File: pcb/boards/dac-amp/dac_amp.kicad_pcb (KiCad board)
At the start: 2 copper layers, 65 x 56 mm, 49 parts, among them J1 I2S_Input, J2 12V_Input, J3 Front_Left, J4 Front_Right, J5 Rear_Left, J6 Rear_Right, J7 40-Pin_GPIO, U1 PCM5142, U2 AMS1117-3.3, U3 TPA3116D2, U4 TPA3116D2

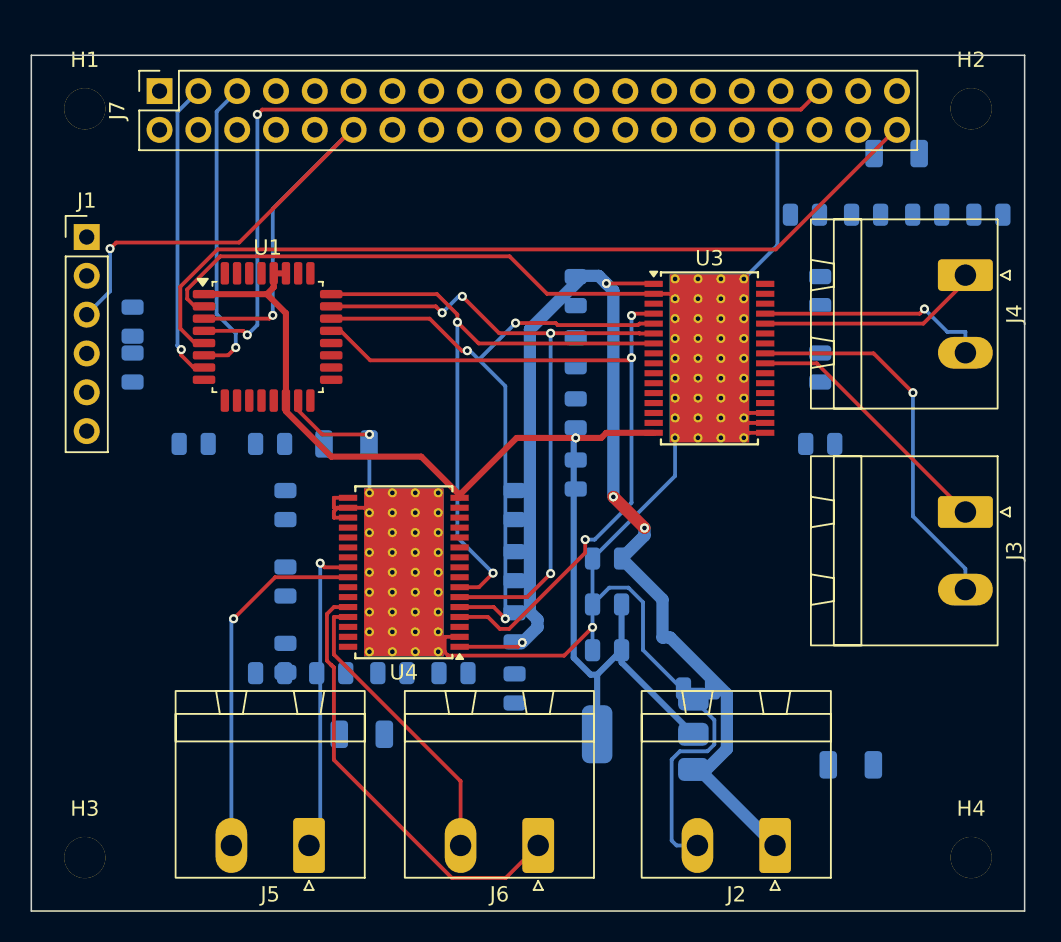
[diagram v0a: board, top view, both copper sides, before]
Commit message: DAC/Amp HAT PCB: Ready for PCBA manufacturing
- PCB fully routed via FreeRouting auto-router
- DRC clean: 0 unconnected pads, 0 errors (warnings are cosmetic)
- Power traces widened: +12V @ 1.0mm, speaker outputs @ 0.75mm
- Thermal vias added under U3 and U4 (6-8 vias each)
- Fiducials added for pick-and-place assembly
- GND copper pour on back layer for thermal dissipation
- BOM with manufacturer part numbers (dac_amp_bom.csv)
- Gerbers and placement files generated for PCBWay

Manufacturing notes:
- Recommend 2oz copper for power handling
- ENIG surface finish for PCBA
- Double-sided assembly (components on front and back)

Co-Authored-By: Claude Opus 4.5 <noreply@anthropic.com>
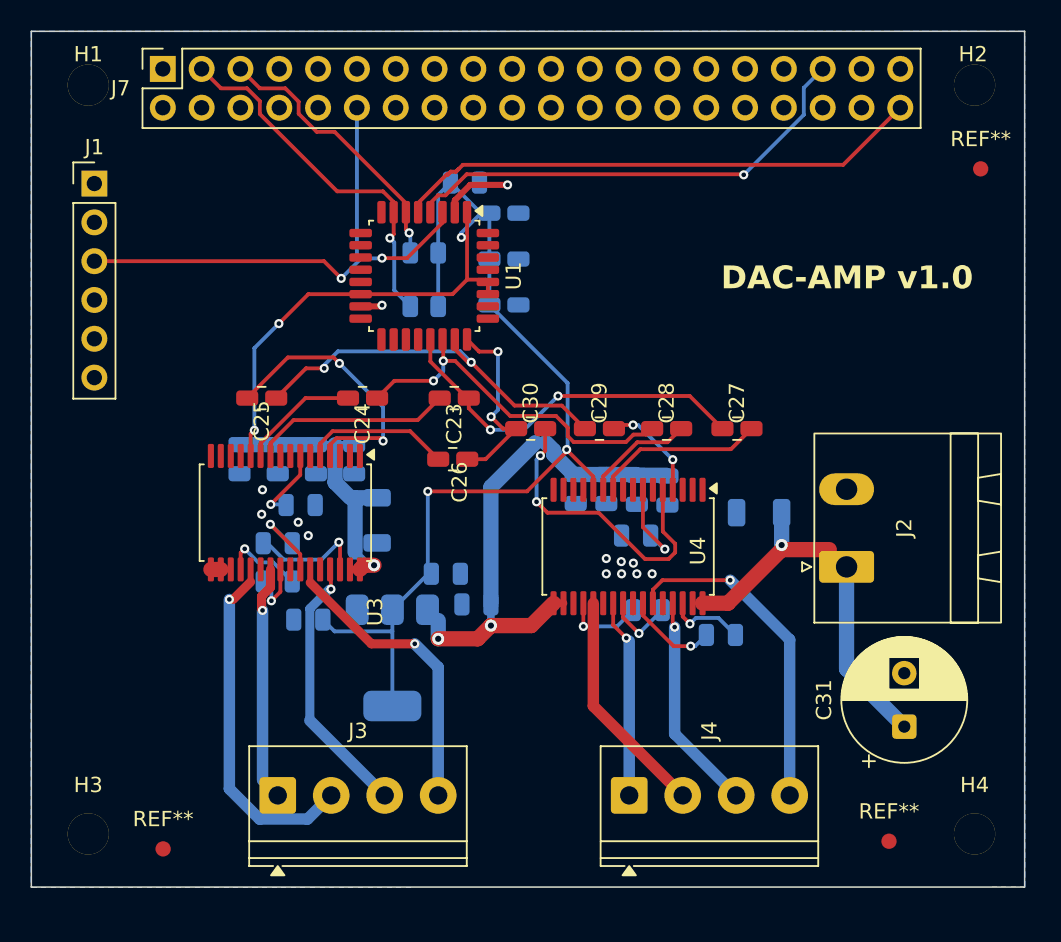
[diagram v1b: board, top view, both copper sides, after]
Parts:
- removed J5: Rear_Left, Connector_Phoenix_MSTB:PhoenixContact_MSTBA_2,5_2-G-5,08_1x02_P5.08mm_Horizontal
- removed J6: Rear_Right, Connector_Phoenix_MSTB:PhoenixContact_MSTBA_2,5_2-G-5,08_1x02_P5.08mm_Horizontal
- added REF**: Fiducial_1mm_Mask2mm, Fiducial:Fiducial_1mm_Mask2mm, F.Cu at (157.5, 86.0)
- added REF**: Fiducial_1mm_Mask2mm, Fiducial:Fiducial_1mm_Mask2mm, F.Cu at (110.0, 86.5)
- added REF**: Fiducial_1mm_Mask2mm, Fiducial:Fiducial_1mm_Mask2mm, F.Cu at (163.5, 42.0)
- C10, C11, C12, C13, C14, C15, C16, C17, C18, C19, C20, C21, C22, C32, C4, C5, C7, C8, C9, R1, R2: moved to F.Cu
- C31: footprint Capacitor_SMD:C_1206_3216Metric -> Capacitor_THT:CP_Radial_D8.0mm_P3.50mm; moved to F.Cu
- C6: footprint Capacitor_SMD:C_1206_3216Metric -> Capacitor_SMD:C_0805_2012Metric; moved to F.Cu
- J3: value Front_Left -> Conn_01x04; footprint Connector_Phoenix_MSTB:PhoenixContact_MSTBA_2,5_2-G-5,08_1x02_P5.08mm_Horizontal -> TerminalBlock_Phoenix:TerminalBlock_Phoenix_PT-1,5-4-3.5-H_1x04_P3.50mm_Horizontal
- J4: value Front_Right -> Conn_01x04; footprint Connector_Phoenix_MSTB:PhoenixContact_MSTBA_2,5_2-G-5,08_1x02_P5.08mm_Horizontal -> TerminalBlock_Phoenix:TerminalBlock_Phoenix_PT-1,5-4-3.5-H_1x04_P3.50mm_Horizontal
- U3, U4: value TPA3116D2 -> TPA3116D2DAD; footprint Package_SO:HTSSOP-32-1EP_6.1x11mm_P0.65mm_EP5.2x11mm_Mask4.11x4.36mm_ThermalVias -> Package_SO:Texas_DAD0032A_HTSSOP-32_6.1x11mm_P0.65mm_TopEP3.71x3.81mm
- moved J3 48.7 mm to (117.5, 83.0), turned to 0 degrees
- moved C14 44.5 mm to (122.5, 61.0), turned to -90 degrees
- moved C13 43.1 mm to (120.0, 61.0), turned to -90 degrees
- moved C12 41.7 mm to (117.5, 61.0), turned to -90 degrees
- moved C19 41.6 mm to (124.0, 65.0), turned to -90 degrees
- moved J4 40.5 mm to (140.5, 83.0), turned to 0 degrees
- moved C11 40.3 mm to (115.0, 61.0), turned to -90 degrees
- moved C7 40.3 mm to (117.5, 69.0), turned to 0 degrees
- moved C8 37.3 mm to (117.5, 66.5), turned to 0 degrees
- moved C21 34.2 mm to (119.0, 64.0)
- moved C20 29.8 mm to (149.0, 64.5), turned to 180 degrees
- moved U3 29.5 mm to (118.0, 64.5), turned to -90 degrees
- moved C2 29.1 mm to (129.8, 42.9), turned to 0 degrees
- moved C10 28.7 mm to (146.5, 72.5), turned to 180 degrees
- moved C9 24.7 mm to (141.7, 70.9), turned to 180 degrees
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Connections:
- C1 pad 1: +12V -> /+12V
- C10 pad 1: (no net) -> /U4_BSPR
- C10 pad 2: (no net) -> /U4_BSNR
- C11 pad 1: (no net) -> /+12V
- C11 pad 2: (no net) -> GND
- C12 pad 1: (no net) -> /+12V
- C12 pad 2: (no net) -> GND
- C13 pad 1: (no net) -> /+12V
- C13 pad 2: (no net) -> GND
- C14 pad 1: (no net) -> /+12V
- C14 pad 2: (no net) -> GND
- C15 pad 1: (no net) -> /+12V
- C15 pad 2: (no net) -> GND
- C16 pad 1: (no net) -> /+12V
- C16 pad 2: (no net) -> GND
- C17 pad 1: (no net) -> /+12V
- C17 pad 2: (no net) -> GND
- C18 pad 1: (no net) -> /+12V
- C18 pad 2: (no net) -> GND
- C19 pad 1: (no net) -> /+12V
- C19 pad 2: (no net) -> GND
- C20 pad 1: (no net) -> /+12V
- C20 pad 2: (no net) -> GND
- C21 pad 1: (no net) -> /U3_GVDD
- C21 pad 2: (no net) -> GND
- C22 pad 1: (no net) -> /U4_GVDD
- C22 pad 2: (no net) -> GND
- C23 pad 1: (no net) -> /DAC_OUTL+
- C23 pad 2: (no net) -> /U3_LINP
- C24 pad 1: (no net) -> /DAC_OUTL-
- C24 pad 2: (no net) -> /U3_LINN
- C25 pad 1: (no net) -> /DAC_OUTR+
- C25 pad 2: (no net) -> /U3_RINP
- C26 pad 1: (no net) -> /DAC_OUTR-
- C26 pad 2: (no net) -> /U3_RINN
- C27 pad 1: (no net) -> /DAC_OUTL+
- C27 pad 2: (no net) -> /U4_LINP
- C28 pad 1: (no net) -> /DAC_OUTL-
- C28 pad 2: (no net) -> /U4_LINN
- C29 pad 1: (no net) -> /DAC_OUTR+
- C29 pad 2: (no net) -> /U4_RINP
- C30 pad 1: (no net) -> /DAC_OUTR-
- C30 pad 2: (no net) -> /U4_RINN
- C31 pad 1: (no net) -> /+12V
- C31 pad 2: (no net) -> GND
- C32 pad 1: (no net) -> +3.3V
- C32 pad 2: (no net) -> GND
- C4 pad 1: (no net) -> +3.3V
- C4 pad 2: (no net) -> GND
- C5 pad 1: (no net) -> +3.3V
- C5 pad 2: (no net) -> GND
- C6 pad 1: (no net) -> +3.3V
- C6 pad 2: (no net) -> GND
- C7 pad 1: (no net) -> /U3_BSPL
- C7 pad 2: (no net) -> /U3_BSNL
- C8 pad 1: (no net) -> /U3_BSPR
- C8 pad 2: (no net) -> /U3_BSNR
- C9 pad 1: (no net) -> /U4_BSPL
- C9 pad 2: (no net) -> /U4_BSNL
- J2 pad 1: +12V -> /+12V
- J3 pad 1: Net-(J3-Pin_1) -> /U3_OUTPL
- J3 pad 2: Net-(J3-Pin_2) -> /U3_OUTNL
- J4 pad 1: Net-(J4-Pin_1) -> /U4_OUTPL
- J4 pad 2: Net-(J4-Pin_2) -> /U4_OUTNL
- R1 pad 1: (no net) -> +3.3V
- R1 pad 2: (no net) -> I2C_SCL
- R2 pad 1: (no net) -> +3.3V
- R2 pad 2: (no net) -> I2C_SDA
- U1 pad 21: Net-(U1-OUTL+) -> /DAC_OUTL+
- U1 pad 22: Net-(U1-OUTL-) -> /DAC_OUTL-
- U1 pad 23: Net-(U1-OUTR+) -> /DAC_OUTR+
- U1 pad 24: Net-(U1-OUTR-) -> /DAC_OUTR-
- U2 pad 3: +12V -> /+12V
- U3 pad 1: +12V -> GND
- U3 pad 10: (no net) -> /U3_LINP
- U3 pad 11: (no net) -> /U3_LINN
- U3 pad 12: (no net) -> +3.3V
- U3 pad 13: (no net) -> GND
- U3 pad 14: (no net) -> GND
- U3 pad 15: (no net) -> GND
- U3 pad 16: +3.3V -> unconnected-(U3-SYNC-Pad16)
- U3 pad 17: GND -> /+12V
- U3 pad 18: GND -> /+12V
- U3 pad 19: GND -> /+12V
- U3 pad 2: GND -> /+12V
- U3 pad 20: (no net) -> /U3_BSNL
- U3 pad 21: (no net) -> /U3_OUTNL
- U3 pad 22: (no net) -> GND
- U3 pad 23: (no net) -> /U3_OUTPL
- U3 pad 24: Net-(J3-Pin_1) -> /U3_BSPL
- U3 pad 25: Net-(J3-Pin_2) -> GND
- U3 pad 26: (no net) -> /U3_BSNR
- U3 pad 27: (no net) -> /U3_OUTNR
- U3 pad 28: Net-(J4-Pin_1) -> GND
- U3 pad 29: Net-(J4-Pin_2) -> /U3_OUTPR
- U3 pad 3: (no net) -> unconnected-(U3-FAULTZ-Pad3)
- U3 pad 30: (no net) -> /U3_BSPR
- U3 pad 31: (no net) -> /+12V
- U3 pad 32: (no net) -> /+12V
- U3 pad 4: Net-(U1-OUTL+) -> /U3_RINP
- U3 pad 5: Net-(U1-OUTL-) -> /U3_RINN
- U3 pad 6: Net-(U1-OUTR+) -> unconnected-(U3-PLIMIT-Pad6)
- U3 pad 7: Net-(U1-OUTR-) -> /U3_GVDD
- U3 pad 8: (no net) -> GND
- U3 pad 9: (no net) -> GND
- U4 pad 1: +12V -> GND
- U4 pad 10: (no net) -> /U4_LINP
- U4 pad 11: (no net) -> /U4_LINN
- U4 pad 12: (no net) -> +3.3V
- U4 pad 13: (no net) -> GND
- U4 pad 14: (no net) -> GND
- U4 pad 15: (no net) -> GND
- U4 pad 16: +3.3V -> unconnected-(U4-SYNC-Pad16)
- U4 pad 17: GND -> /+12V
- U4 pad 18: GND -> /+12V
- U4 pad 19: GND -> /+12V
- U4 pad 2: GND -> /+12V
- U4 pad 20: (no net) -> /U4_BSNL
- U4 pad 21: (no net) -> /U4_OUTNL
- U4 pad 22: (no net) -> GND
- U4 pad 23: (no net) -> /U4_OUTPL
- U4 pad 24: Net-(J5-Pin_1) -> /U4_BSPL
- U4 pad 25: Net-(J5-Pin_2) -> GND
- U4 pad 26: (no net) -> /U4_BSNR
- U4 pad 27: (no net) -> /U4_OUTNR
- U4 pad 28: Net-(J6-Pin_1) -> GND
- U4 pad 29: Net-(J6-Pin_2) -> /U4_OUTPR
- U4 pad 3: (no net) -> unconnected-(U4-FAULTZ-Pad3)
- U4 pad 30: (no net) -> /U4_BSPR
- U4 pad 31: (no net) -> /+12V
- U4 pad 32: (no net) -> /+12V
- U4 pad 4: Net-(U1-OUTL+) -> /U4_RINP
- U4 pad 5: Net-(U1-OUTL-) -> /U4_RINN
- U4 pad 6: Net-(U1-OUTR+) -> unconnected-(U4-PLIMIT-Pad6)
- U4 pad 7: Net-(U1-OUTR-) -> /U4_GVDD
- U4 pad 8: (no net) -> GND
- U4 pad 9: (no net) -> GND
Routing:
- net GND: track 219.1 -> 6.08 mm, vias 2 -> 13
- net +12V: track 80.0 -> 0.00 mm, vias 4 -> 0
- net /+12V: track 0.00 -> 80.0 mm, vias 0 -> 4
- net Net-(U1-OUTL+): track 49.8 -> 0.00 mm, vias 3 -> 0
- net Net-(U1-OUTR+): track 45.0 -> 0.00 mm, vias 4 -> 0
- net Net-(U1-OUTL-): track 44.3 -> 0.00 mm, vias 3 -> 0
- net Net-(U1-OUTR-): track 42.7 -> 0.00 mm, vias 2 -> 0
- net Net-(J6-Pin_1): track 29.0 -> 0.00 mm
- net /DAC_OUTR+: track 0.00 -> 25.8 mm, vias 0 -> 2
- net Net-(J3-Pin_2): track 25.0 -> 0.00 mm, vias 1 -> 0
- net /DAC_OUTL+: track 0.00 -> 24.6 mm, vias 0 -> 2
- net I2S_LRCK: track 55.1 -> 31.0 mm, vias 2 -> 1
- net /DAC_OUTL-: track 0.00 -> 23.7 mm, vias 0 -> 2
- net Net-(J5-Pin_2): track 23.5 -> 0.00 mm, vias 1 -> 0
- net /U3_OUTNL: track 0.00 -> 23.2 mm, vias 0 -> 1
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- added copper zone on B.Cu, net GND
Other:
- board text added: "DAC-AMP v1.0"
